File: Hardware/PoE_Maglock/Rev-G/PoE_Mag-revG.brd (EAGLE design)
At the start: 66.4 x 45.4 mm, 85 parts, among them IC2 ATMEGA32U4-MU, J2 1X2-3.5MM, J3 1X2-3.5MM, J4 1X2-3.5MM, J5 1X2-3.5MM, J6 10103594-0001LF, Q1 35A/25V/8.5mΩ, Q3 35A/25V/8.5mΩ, Q5 35A/25V/8.5mΩ, Q6 35A/25V/8.5mΩ, SW1 SPST_TACT-KMR2, U4 W5500, X2 J1011FHY931147C, Y4 8MHz

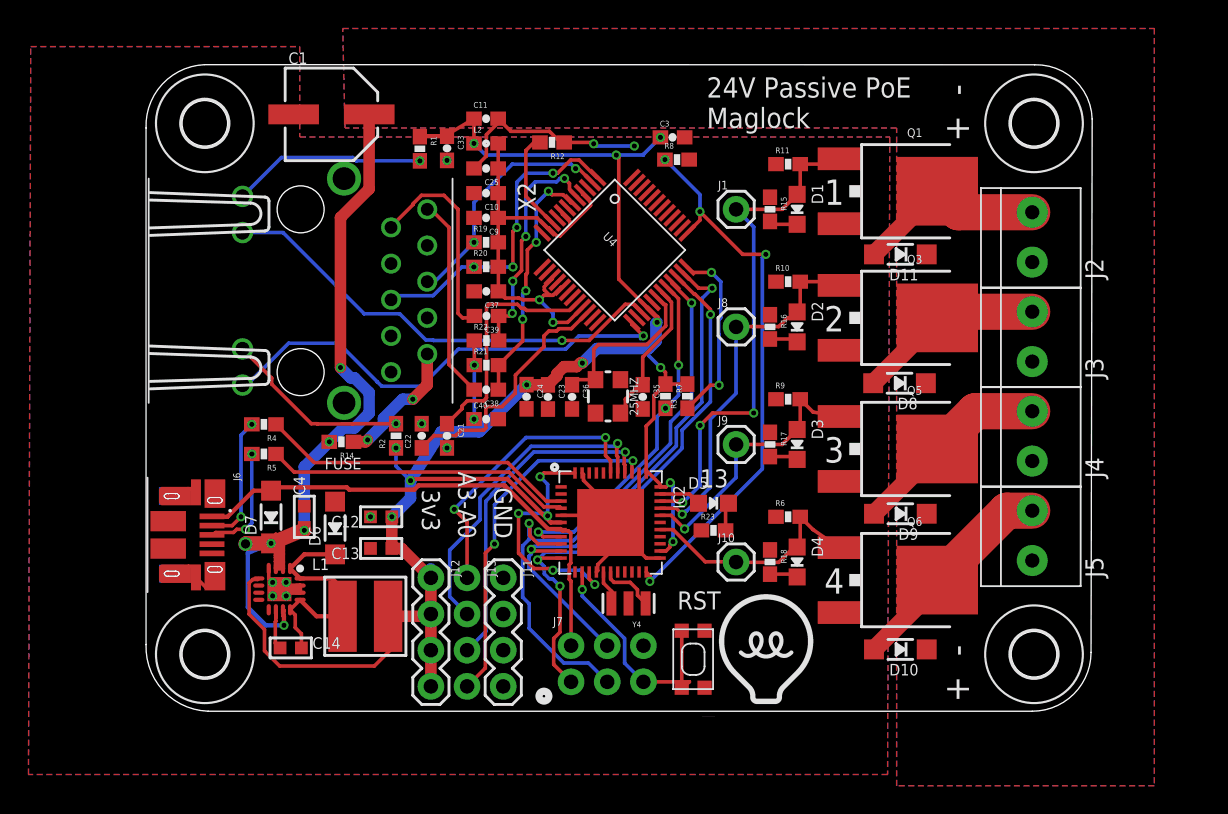
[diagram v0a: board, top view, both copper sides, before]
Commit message: HEEP-1046 Moved Bottom Pour Up, Added Vias below 32u4, Spaced out Mag Terminals, Added + - to front of mag terminals, bolded mag num silk
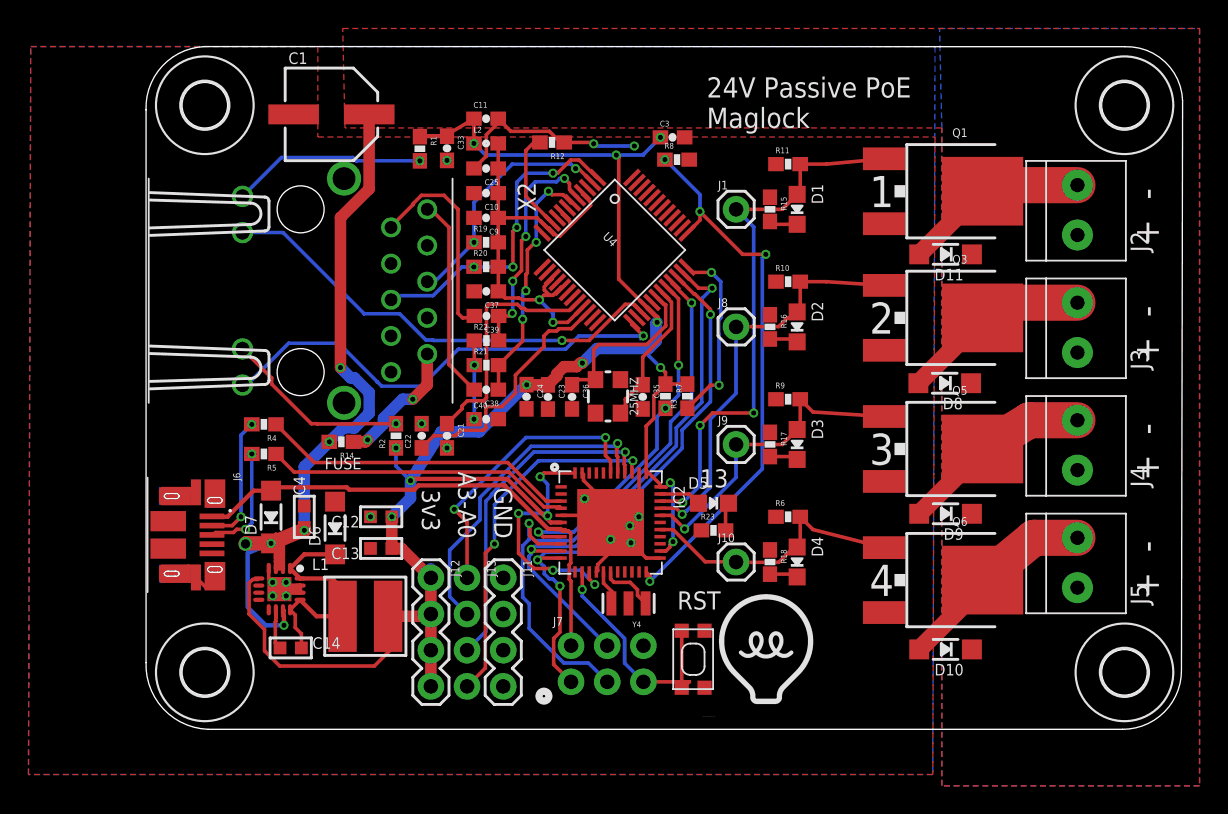
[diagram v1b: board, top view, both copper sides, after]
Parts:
- moved H4 6.48 mm to (73.1, 3.05)
- moved H1 6.48 mm to (73.1, 42.9)
- moved J2 3.70 mm to (69.8, 35.6)
- moved J5 3.70 mm to (69.8, 10.8)
- moved J3 3.24 mm to (69.8, 27.3)
- moved J4 3.24 mm to (69.8, 19.1)
- moved D10 3.17 mm to (60.6, 4.66)
- moved D11 3.17 mm to (60.6, 32.4)
- moved D8 3.17 mm to (60.5, 23.4)
- moved D9 3.17 mm to (60.6, 14.2)
- moved Q1 3.17 mm to (61.6, 36.8)
- moved Q3 3.17 mm to (61.6, 27.9)
- moved Q5 3.17 mm to (61.6, 18.7)
- moved Q6 3.17 mm to (61.6, 9.53)
- moved H2 1.27 mm to (8.57, 3.05)
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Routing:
- net GND: track 42.3 -> 48.9 mm, vias 10 -> 15
- net EN3: track 19.6 -> 22.8 mm
- net EN2: track 26.2 -> 29.3 mm
- net EN1: track 36.2 -> 39.4 mm
- net EN4: track 16.7 -> 19.7 mm
- net DRAIN4: track 15.4 -> 14.4 mm
- net DRAIN1: track 13.6 -> 13.0 mm
- net DRAIN2: track 13.3 -> 13.8 mm
- net DRAIN3: track 15.1 -> 14.6 mm
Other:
- board size 66.4 x 45.4 mm -> 72.8 x 47.9 mm

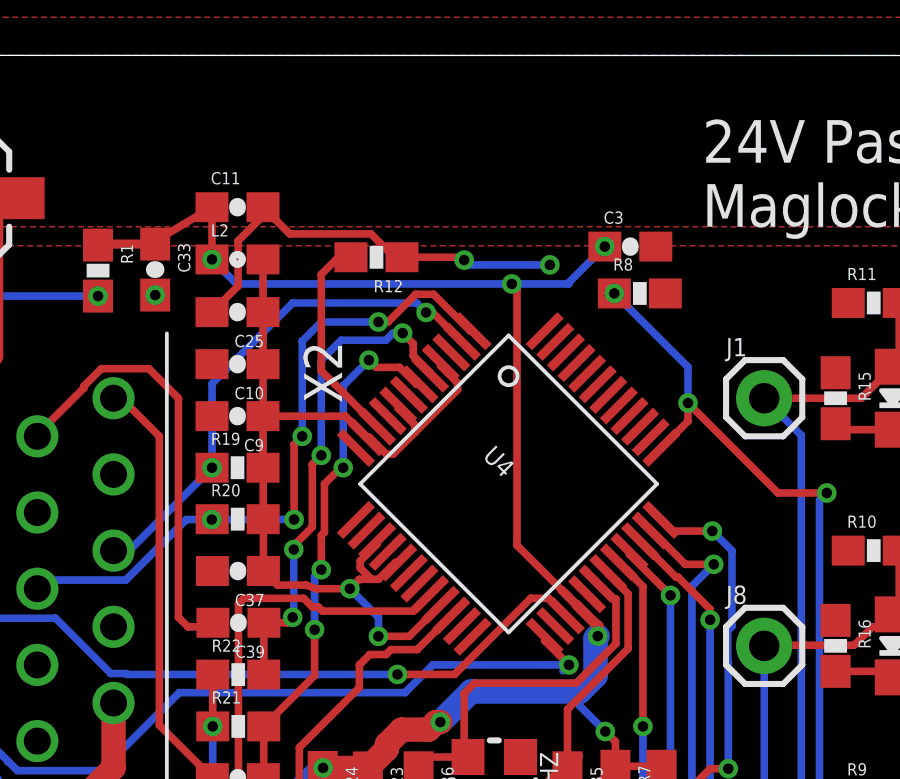
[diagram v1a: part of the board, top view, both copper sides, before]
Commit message: HEEP-1046 Improved heat dissapation on Wiznet
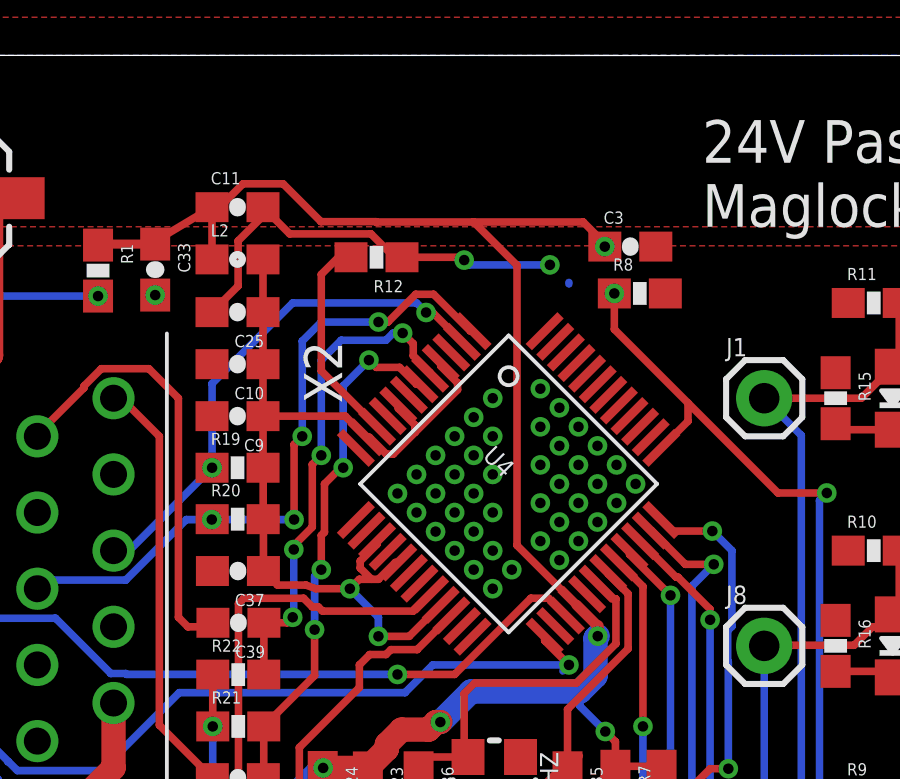
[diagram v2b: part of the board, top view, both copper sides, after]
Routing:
- net +3V3: track 146.6 -> 149.6 mm, vias 17 -> 15
- net WIZ_RST: vias 4 -> 3
- net GND: vias 15 -> 57
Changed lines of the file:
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@@
 <wire x1="35.3977625" y1="15.24" x2="35.2425" y2="15.24" width="0.1524" layer="1"/>
 <via x="35.2425" y="15.24" extent="1-16" drill="0.35"/>
+<via x="33.655" y="32.385" extent="1-16" drill="0.35"/>
+<via x="34.29" y="33.02" extent="1-16" drill="0.35"/>
+<via x="34.925" y="33.655" extent="1-16" drill="0.35"/>
+<via x="35.56" y="34.29" extent="1-16" drill="0.35"/>
+<via x="36.195" y="34.925" extent="1-16" drill="0.35"/>
+<via x="36.83" y="35.56" extent="1-16" drill="0.35"/>
+<via x="36.83" y="34.29" extent="1-16" drill="0.35"/>
+<via x="36.195" y="33.655" extent="1-16" drill="0.35"/>
+<via x="35.56" y="33.02" extent="1-16" drill="0.35"/>
+<via x="34.925" y="32.385" extent="1-16" drill="0.35"/>
+<via x="34.29" y="31.75" extent="1-16" drill="0.35"/>
+<via x="34.925" y="31.115" extent="1-16" drill="0.35"/>
+<via x="35.56" y="31.75" extent="1-16" drill="0.35"/>
+<via x="36.195" y="32.385" extent="1-16" drill="0.35"/>
+<via x="36.83" y="33.02" extent="1-16" drill="0.35"/>
+<via x="36.83" y="31.75" extent="1-16" drill="0.35"/>
+<via x="36.195" y="31.115" extent="1-16" drill="0.35"/>
+<via x="35.56" y="30.48" extent="1-16" drill="0.35"/>
+<via x="36.195" y="29.845" extent="1-16" drill="0.35"/>
+<via x="36.83" y="30.48" extent="1-16" drill="0.35"/>
+<via x="36.83" y="29.21" extent="1-16" drill="0.35"/>
+<via x="37.465" y="29.845" extent="1-16" drill="0.35"/>
+<via x="38.4175" y="30.7975" extent="1-16" drill="0.35"/>
+<via x="39.0525" y="30.1625" extent="1-16" drill="0.35"/>
+<via x="39.6875" y="30.7975" extent="1-16" drill="0.35"/>
+<via x="39.0525" y="31.4325" extent="1-16" drill="0.35"/>
+<via x="38.4175" y="32.0675" extent="1-16" drill="0.35"/>
+<via x="39.0525" y="32.7025" extent="1-16" drill="0.35"/>
+<via x="38.4175" y="33.3375" extent="1-16" drill="0.35"/>
+<via x="39.0525" y="33.9725" extent="1-16" drill="0.35"/>
+<via x="38.4175" y="34.6075" extent="1-16" drill="0.35"/>
+<via x="39.0525" y="35.2425" extent="1-16" drill="0.35"/>
+<via x="38.4175" y="35.8775" extent="1-16" drill="0.35"/>
+<via x="39.6875" y="34.6075" extent="1-16" drill="0.35"/>
+<via x="39.6875" y="33.3375" extent="1-16" drill="0.35"/>
+<via x="39.6875" y="32.0675" extent="1-16" drill="0.35"/>
+<via x="40.3225" y="31.4325" extent="1-16" drill="0.35"/>
+<via x="40.9575" y="32.0675" extent="1-16" drill="0.35"/>
+<via x="40.3225" y="32.7025" extent="1-16" drill="0.35"/>
+<via x="40.9575" y="33.3375" extent="1-16" drill="0.35"/>
+<via x="40.3225" y="33.9725" extent="1-16" drill="0.35"/>
+<via x="41.5925" y="32.7025" extent="1-16" drill="0.35"/>
+<wire x1="40.9575" y1="32.0675" x2="41.5925" y2="32.7025" width="0" layer="19" extent="1-1"/>
 </signal>
 <signal name="RD-">
@@
 <wire x1="23.01875" y1="15.28375" x2="23.01875" y2="16.5057" width="0.8128" layer="16"/>
 <wire x1="27.472175" y1="41.927496875" x2="27.472175" y2="40.187434375" width="0.254" layer="1"/>
-<via x="27.472175" y="40.187434375" extent="1-16" drill="0.35"/>
-<wire x1="27.472175" y1="40.187434375" x2="28.289609375" y2="39.37" width="0.254" layer="16"/>
-<wire x1="28.289609375" y1="39.37" x2="37.465" y2="39.37" width="0.254" layer="16"/>
-<wire x1="37.465" y1="39.37" x2="39.37" y2="39.37" width="0.254" layer="16"/>
 <wire x1="39.37" y1="39.37" x2="39.37" y2="39.41821875" width="0.254" layer="16"/>
-<wire x1="39.37" y1="39.41821875" x2="40.5656125" y2="40.61383125" width="0.254" layer="16"/>
 <via x="40.5656125" y="40.61383125" extent="1-16" drill="0.35"/>
-<via x="37.465" y="39.37" extent="1-16" drill="0.35"/>
-<wire x1="37.63935" y1="30.65435" x2="37.63935" y2="39.19565" width="0.254" layer="1"/>
-<wire x1="37.63935" y1="39.19565" x2="37.465" y2="39.37" width="0.254" layer="1"/>
+<wire x1="37.63935" y1="30.65435" x2="37.63935" y2="39.9894" width="0.254" layer="1"/>
 <wire x1="21.44375" y1="6.985" x2="24.28875" y2="6.985" width="0.8128" layer="1"/>
 <wire x1="24.28875" y1="6.985" x2="24.4475" y2="7.14375" width="0.8128" layer="1"/>
 <wire x1="23.673640625" y1="40.664415625" x2="23.707028125" y2="40.697803125" width="0.3048" layer="1"/>
 <wire x1="23.707028125" y1="40.697803125" x2="25.41749375" y2="40.697803125" width="0.3048" layer="1"/>
+<wire x1="27.472175" y1="41.927496875" x2="27.727046875" y2="41.927496875" width="0.254" layer="1"/>
+<wire x1="27.727046875" y1="41.927496875" x2="28.50644375" y2="42.70689375" width="0.254" layer="1"/>
+<wire x1="28.50644375" y1="42.70689375" x2="29.84185625" y2="42.70689375" width="0.254" layer="1"/>
+<wire x1="31.10409375" y1="41.44465625" x2="32.939396875" y2="41.44465625" width="0.254" layer="1"/>
+<wire x1="32.939396875" y1="41.44465625" x2="32.950303125" y2="41.43375" width="0.254" layer="1"/>
+<wire x1="32.950303125" y1="41.43375" x2="36.195" y2="41.43375" width="0.254" layer="1"/>
+<wire x1="36.195" y1="41.43375" x2="39.84625" y2="41.43375" width="0.254" layer="1"/>
+<wire x1="29.84185625" y1="42.70689375" x2="31.10409375" y2="41.44465625" width="0.254" layer="1"/>
+<wire x1="39.84625" y1="41.43375" x2="40.5656125" y2="40.7143875" width="0.254" layer="1"/>
+<wire x1="40.5656125" y1="40.7143875" x2="40.5656125" y2="40.61383125" width="0.254" layer="1"/>
+<wire x1="36.195" y1="41.43375" x2="37.63935" y2="39.9894" width="0.254" layer="1"/>
+<wire x1="40.5656125" y1="40.61383125" x2="39.37" y2="39.41821875" width="0" layer="19" extent="1-16"/>
 </signal>
 <signal name="13">
@@
 <wire x1="42.4501375" y1="33.90458125" x2="43.33875" y2="34.79319375" width="0.254" layer="1"/>
 <wire x1="43.33875" y1="34.79319375" x2="43.33875" y2="35.40125" width="0.254" layer="1"/>
-<via x="43.33875" y="35.40125" extent="1-16" drill="0.35"/>
-<wire x1="43.33875" y1="35.40125" x2="43.33875" y2="36.5968625" width="0.254" layer="16"/>
-<wire x1="43.33875" y1="36.5968625" x2="40.8831125" y2="39.0525" width="0.254" layer="16"/>
 <via x="40.8831125" y="39.0525" extent="1-16" drill="0.35"/>
 <wire x1="39.5665125" y1="10.09625" x2="39.81904375" y2="9.84371875" width="0.254" layer="1"/>
@@
 <wire x1="39.81904375" y1="9.4324875" x2="47.722125" y2="17.33556875" width="0.254" layer="16"/>
 <wire x1="47.722125" y1="17.33556875" x2="47.722125" y2="32.157240625" width="0.254" layer="16"/>
+<wire x1="43.33875" y1="35.40125" x2="40.8831125" y2="37.8568875" width="0.254" layer="1"/>
+<wire x1="40.8831125" y1="37.8568875" x2="40.8831125" y2="39.0525" width="0.254" layer="1"/>
 </signal>
 <signal name="SCSN_WIZ">

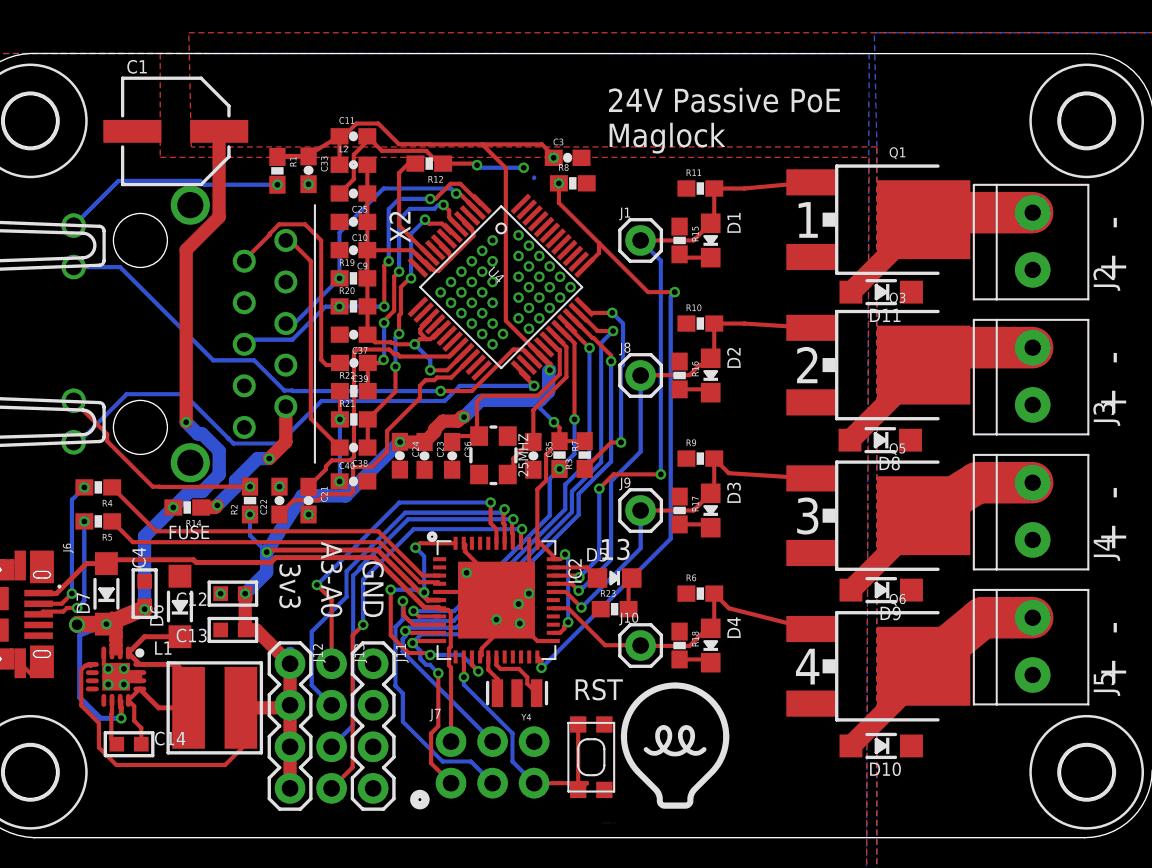
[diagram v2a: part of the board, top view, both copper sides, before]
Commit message: HEEP-1046 Changed 10uF buck cap to 0805
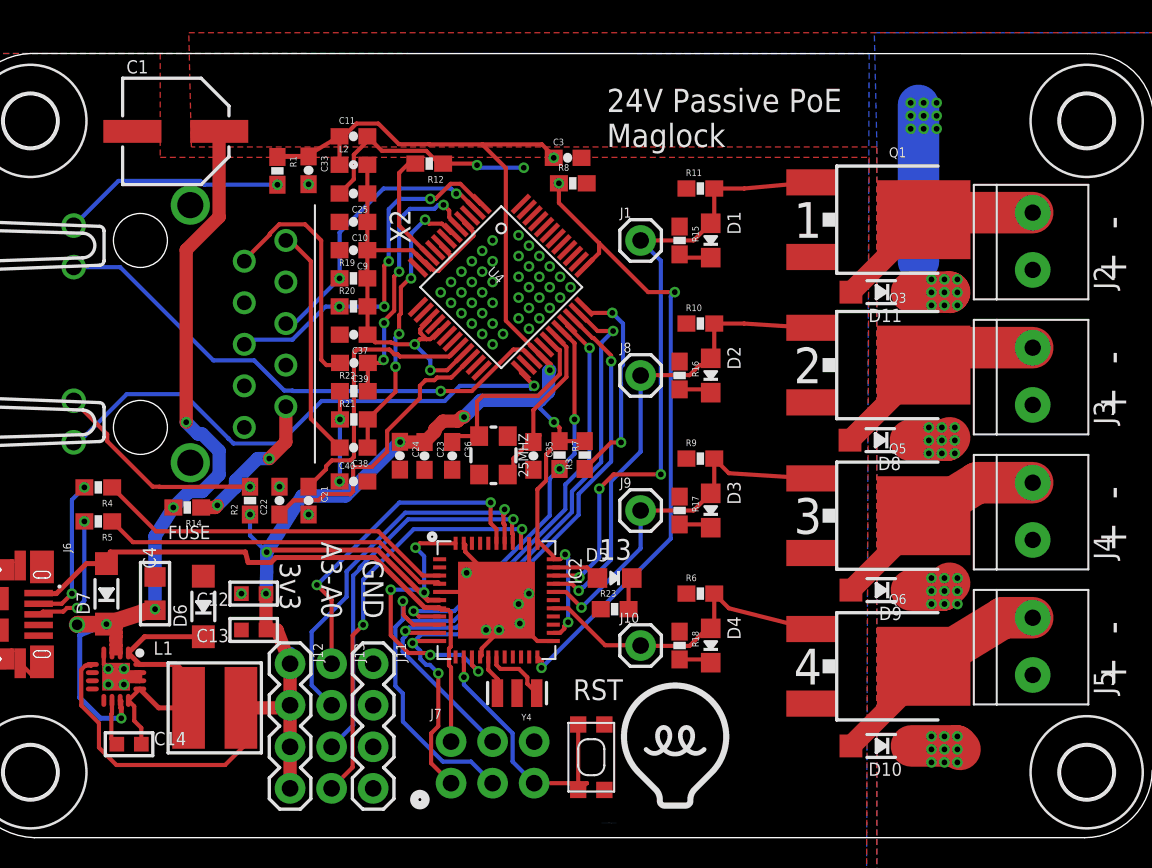
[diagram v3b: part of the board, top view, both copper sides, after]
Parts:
- C4: value 10µF 25V -> 10µF 50V; device microbuilder:0603-MINI -> microbuilder:_0805
- moved D6 1.43 mm to (19.1, 13.2)
- moved C12 1.27 mm to (22.2, 14.0)
- moved C13 1.27 mm to (22.2, 11.7)
- moved C4 0.63 mm to (16.2, 14.0)
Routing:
- net VBAT: track 58.5 -> 77.9 mm, vias 6 -> 51
- net GND: track 48.9 -> 50.3 mm, vias 57 -> 58
- net N$16: track 17.2 -> 18.7 mm
- net +3V3: track 149.6 -> 148.3 mm
- net VBUS: track 36.3 -> 37.2 mm
